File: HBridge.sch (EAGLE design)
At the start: 51 parts, among them IC1 74LS08D, IC2 A4954, J1 Inputs, J10 JUMPER_PTH, J11 PWM mode, J12 Fixed mode, J13 Ground, J14 5V, J15 Digital_8_13, J16 Analog, J17 Digital_0_7, J2 JUMPER_PTH, J3 JUMPER_PTH, J4 PWM mode, J5 Fixed mode, J6 Power, J7 Output A, J8 Output B, J9 JUMPER_PTH

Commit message: foo
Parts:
- removed C9: 100nF, freetronics:CAP0603
- removed J10, J9: JUMPER_PTH, freetronics-luke:JUMPER_PTH
- removed J11: PWM mode, freetronics-luke:JUMPER_PTH
- removed J12: Fixed mode, freetronics-luke:JUMPER_PTH
- removed J13: Ground, freetronics-master-v1:M08STD
- removed J14: 5V, freetronics-master-v1:M08STD
- removed J15: Digital_8_13, freetronics:M08
- removed J16: Analog, freetronics:M06SIP
- removed J17: Digital_0_7, freetronics:M08
- removed R10, R8, R9: 1k, freetronics-master-v1:RESISTOR0603
- removed R11, R12: 0.25R 1W, rcl:R-EU_R2010
- removed R13: 2K2, freetronics:RESISTOR0603
- removed R14: 10K, freetronics:RESISTOR0603
- removed S2: SWITCH, freetronics:TAC_SWITCHSMD
- added JP2: +5V, SparkFun:M07
- added JP3: (no value), freetronics-master-v1:M02PTH
- added RN1, RN2: 1K, freetronics-master-v1:4R-NCAY16
- added SJ1: Ch1 Fixed Current Select, freetronics-master-v1:SJ2W
- added SJ2: Ch2 Fixed Current Select, freetronics-master-v1:SJ2W
- added SJ3: Ch1 Fixed/PWM select, freetronics-master-v1:SJ2W
- added SJ4: Ch2 Fixed/PWM select, freetronics-master-v1:SJ2W
- C3: value 100 uF -> 100nF; device rcl:CPOL-EUE3.5-8 -> freetronics-master-v1:CAP0603
- C5: value 100nF -> 100 uF; device freetronics-master-v1:CAP0603 -> freetronics-master-v1:CAP_POLE
- IC1: value 74LS08D -> 74HC08D
- J1: value Inputs -> In 3/4; device freetronics-master-v1:M08STD -> freetronics-master-v1:M04PTH
- J2: value JUMPER_PTH -> Power; device freetronics-luke:JUMPER_PTH -> con-wago-508:W237-02P
- J3: value JUMPER_PTH -> In 1/2; device freetronics-luke:JUMPER_PTH -> freetronics-master-v1:M04PTH
- J4: value PWM mode -> Output A; device freetronics-luke:JUMPER_PTH -> con-wago-508:W237-02P; OC_FARNELL (none) -> unknown; OC_NEWARK (none) -> unknown
- J5: value Fixed mode -> Output B; device freetronics-luke:JUMPER_PTH -> con-wago-508:W237-02P; OC_FARNELL (none) -> unknown; OC_NEWARK (none) -> unknown
- J6: value Power -> Digital_8_13; device con-wago-508:W237-02P -> freetronics:M08
- J7: value Output A -> Analog; device con-wago-508:W237-02P -> freetronics:M06SIP; OC_FARNELL unknown -> (none); OC_NEWARK unknown -> (none)
- J8: value Output B -> Digital_0_7; device con-wago-508:W237-02P -> freetronics:M08; OC_FARNELL unknown -> (none); OC_NEWARK unknown -> (none)
- JP1: value SWITCH -> Gnd; device freetronics:M01PTH -> SparkFun:M07
- R1: value 1k -> 2K2
- R2: value 2k2 -> 2K2
- R3, R4: value 1k -> 10k
- R5, R6: value 1k -> 0.25R 1W; device freetronics-master-v1:RESISTOR0603 -> rcl:R-EU_R2010
- R7: value 2k2 -> 2K2; device freetronics-master-v1:RESISTOR0603 -> freetronics:RESISTOR0603
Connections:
- removed net N$249: JP1.1, R14.2, S2.3, S2.4
- removed net N$66: J10.2, R7.1
- removed net N$67: J10.1, J12.1, J9.1, R10.2
- removed net N$68: J9.2, R6.1
- removed net N$69: C5.1, J11.2, R9.2
- removed net N$83: C4.1, R8.2, R9.1
- new net N$1: RN2D.1, SJ2.2, SJ4.3
- new net N$2: C4.1, RN2B.1, SJ4.1
- new net N$20: RN2C.2, SJ2.3
- new net N$3: C3.1, RN2A.2, RN2B.2
- new net N$4: R1.1, SJ1.1
- net +5V: now also JP2.1, JP2.2, JP2.3, JP2.4, JP2.5, JP2.6, JP2.7, RN1C.1, RN2C.1; no longer C9.1, J14.1, J14.2, J14.3, J14.4, J14.5, J14.6, J14.7, J14.8, R6.2, R7.2, S2.1, S2.2
- net A0: now also J7.1; no longer J16.1
- net A1: now also J7.2; no longer J16.2
- net A2: now also J7.3; no longer J16.3
- net A3: now also J7.4; no longer J16.4
- net A4: now also J7.5; no longer J16.5
- net A5: now also J7.6; no longer J16.6
- net AREF: now also J6.8; no longer J15.8
- net D0_RX: now also J8.1; no longer J17.1
- net D10: now also J6.3; no longer J15.3
- net D11_MOSI: now also J6.4; no longer J15.4
- net D12_MISO: now also J6.5; no longer J15.5
- net D13_SCK: now also J6.6; no longer J15.6
- net D1_TX: now also J8.2; no longer J17.2
- net D2: now also J8.3; no longer J17.3
- net D3: now also J8.4; no longer J17.4
- net D4: now also J8.5; no longer J17.5
- net D5: now also J8.6; no longer J17.6
- net D6: now also J8.7; no longer J17.7
- net D7: now also J8.8; no longer J17.8
- net D8: now also J6.1; no longer J15.1
- net D9: now also J6.2; no longer J15.2
- net GND: now also C3.2, C5.-, J2-2.KL, J6.7, JP1.1, JP1.2, JP1.3, JP1.4, JP1.5, JP1.6, JP1.7, R3.1, R4.1, R6.1, R7.2, RN1D.2, RN2D.2; no longer C3.-, C5.2, C9.2, J13.1, J13.2, J13.3, J13.4, J13.5, J13.6, J13.7, J13.8, J15.7, J6-2.KL, R10.1, R11.1, R12.1, R13.2, R14.1
- net IN1: now also J3.1; no longer J1.1
- net IN2: now also J3.2; no longer J1.2
- net IN3: now also J1.1; no longer J1.3
- net IN4: now also J1.2; no longer J1.4
- net N$10: now also J4-2.KL; no longer J7-2.KL
- net N$11: now also J5-1.KL; no longer J8-1.KL
- net N$12: now also J5-2.KL; no longer J8-2.KL
- net N$13: now also R5.2; no longer R11.2
- net N$14: now also R6.2; no longer R12.2
- net N$15: now also RN1C.2, SJ1.3; no longer J3.2, R2.1
- net N$16: now also RN1D.1, SJ1.2, SJ3.3; no longer J2.1, J3.1, J5.1, R5.2
- net N$17: now also R2.1, SJ2.1; no longer J2.2, R1.1
- net N$18: now also RN1B.1, SJ3.1; no longer J4.2, R4.2
- net N$19: now also RN1A.2, RN1B.2; no longer R3.2, R4.1
- net N$248: now also R7.1; no longer R13.1
- net N$9: now also J4-1.KL; no longer J7-1.KL
- net PWM12: now also J3.3, R3.2; no longer J1.5
- net PWM34: now also J1.3, R4.2; no longer J1.6
- net REF_PWM_12: now also J3.4, RN1A.1; no longer J1.7, R3.1
- net REF_PWM_34: now also J1.4, RN2A.1; no longer J1.8, R8.1
- net VBB: now also C5.+, J2-1.KL, JP3.2; no longer C3.+, J6-1.KL
- net VIN: now also JP3.1
- net VREF12: now also SJ3.2; no longer J4.1, J5.2
- net VREF34: now also SJ4.2; no longer J11.1, J12.2
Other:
- note added: "1-2-3: 2.96V, I = 1.19A"
- note added: "1-2: 1.56V, I = 625mA"
- note added: "1k resistor networks: Small SMD 4-way resistor pack, SAME package footprint as EM."
- note added: "2-3: 2.5V, I = 1A"
- note added: "I limit = Vref / (0.25 ohms * 10)"
- note removed: "Both in: 2.96 V"
- note removed: "C3: Large through-hole electrolytic"
- note removed: "J12 in: 1.56 V"
- note removed: "J13 in: 2.5 V"
- note removed: "J8 in: 1.56 V"
- note removed: "J9 in: 2.5 V"
- moved on the sheet: C1, C2, C4, C6, C7, C8, IC1A, IC1B, IC1C, IC1D, IC1P, IC2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

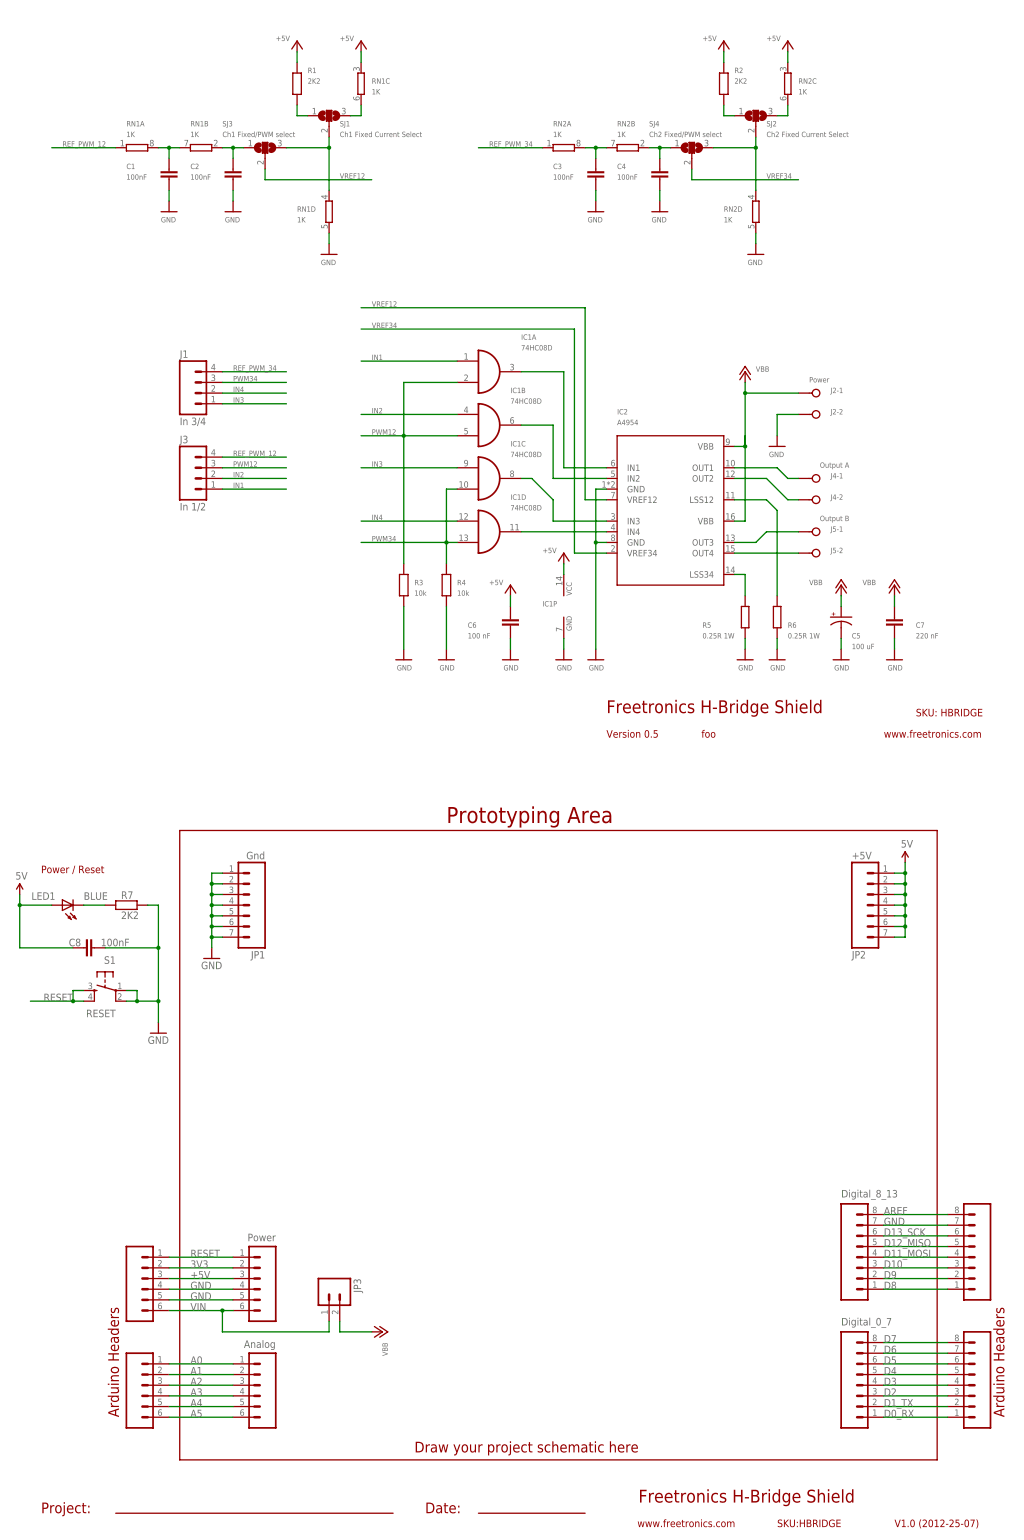
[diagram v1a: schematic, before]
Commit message: Added ICSP header for R3
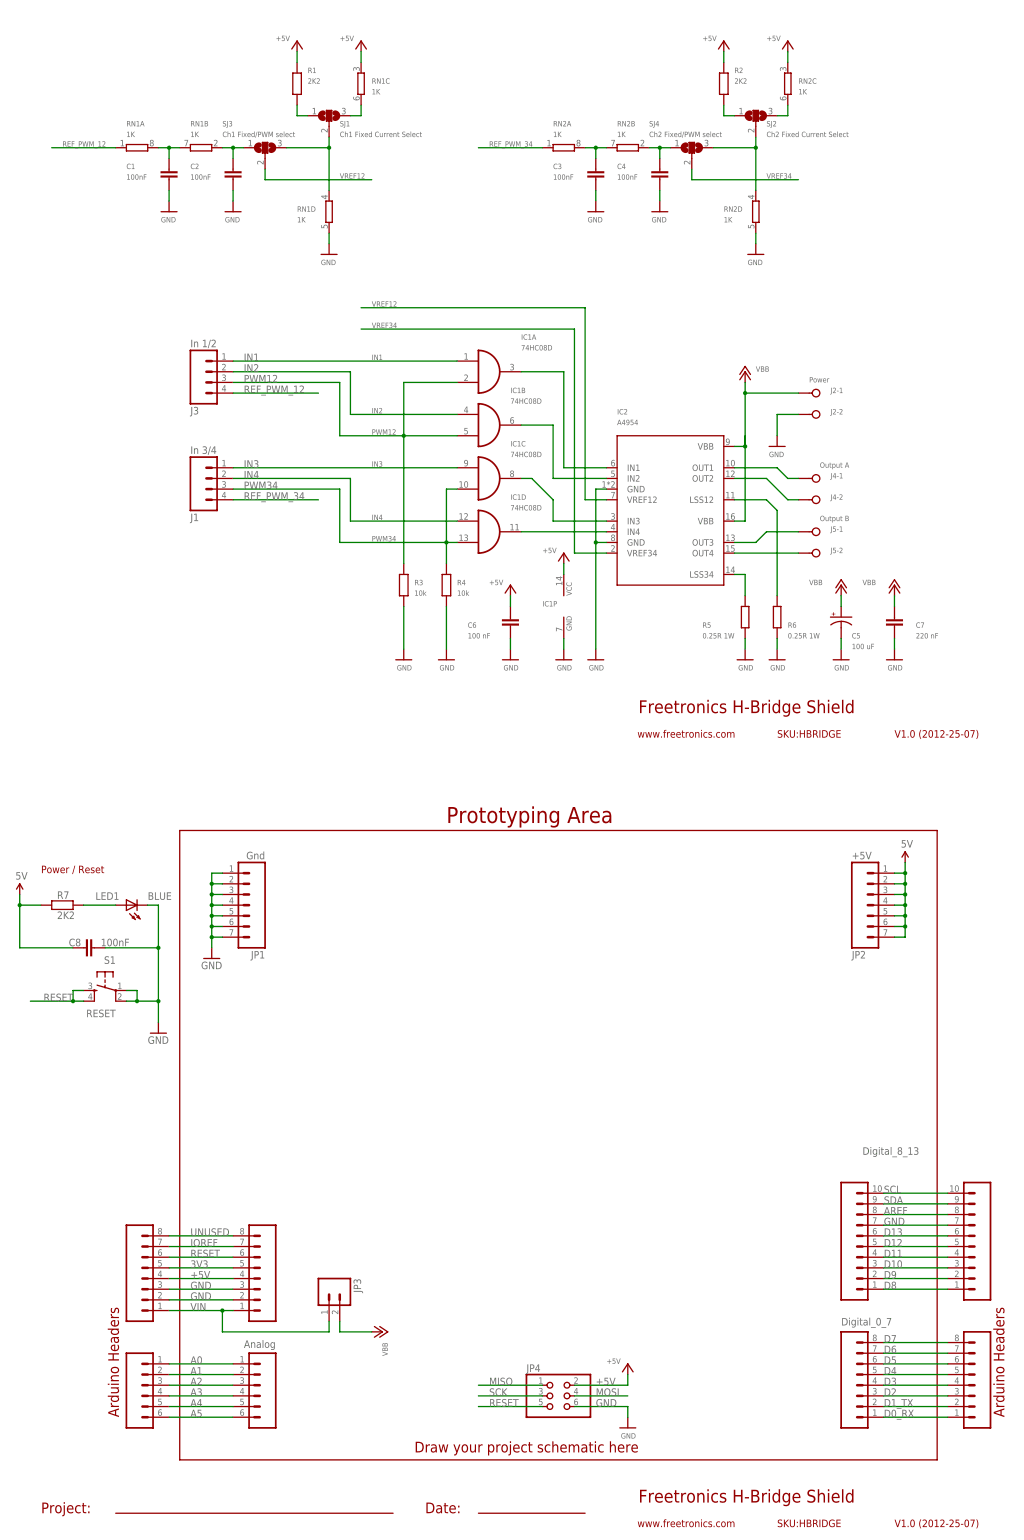
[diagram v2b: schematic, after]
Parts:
- removed POWER, SLP: Power, freetronics:M06SIP
- added JP4: (no value), freetronics-master-v1:PINHD-2X3
- added SL4, SL5: Digital_0_7, freetronics:M08
- J6, SL1: device freetronics:M08 -> freetronics-original:M100.1
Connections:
- net D11_MOSI renamed D11
- net D12_MISO renamed D12
- net D13_SCK renamed D13
- removed net N$248: LED1.C, R7.1
- new net IOREF: SL4.7, SL5.7
- new net MISO: JP4.1
- new net MOSI: JP4.4
- new net N$22: LED1.A, R7.2
- new net SCK: JP4.3
- new net SCL: J6.10, SL1.10
- new net SDA: J6.9, SL1.9
- new net UNUSED: SL4.8, SL5.8
- net +5V: now also JP4.2, R7.1, SL4.4, SL5.4; no longer LED1.A, POWER.3, SLP.3
- net 3V3: now also SL4.5, SL5.5; no longer POWER.2, SLP.2
- net GND: now also JP4.6, LED1.C, SL4.2, SL4.3, SL5.2, SL5.3; no longer POWER.4, POWER.5, R7.2, SLP.4, SLP.5
- net RESET: now also JP4.5, SL4.6, SL5.6; no longer POWER.1, SLP.1
- net VIN: now also SL4.1, SL5.1; no longer POWER.6, SLP.6
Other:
- note removed: "SKU: HBRIDGE"
- note removed: "Version 0.5"
- note removed: "foo"
- moved on the sheet: J1, J3, LED1, R7

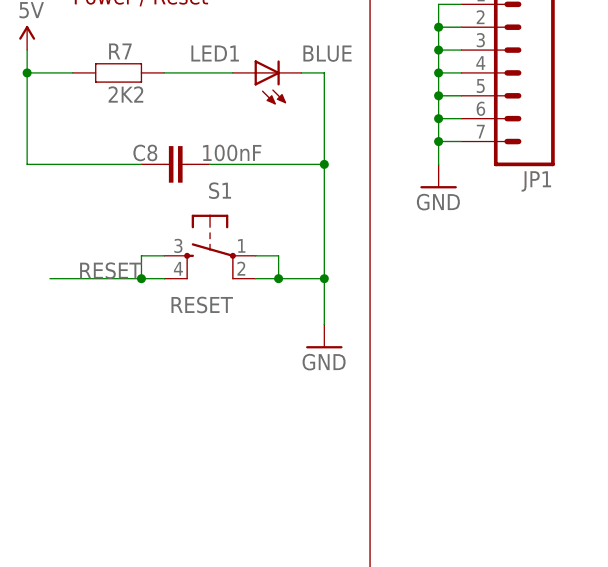
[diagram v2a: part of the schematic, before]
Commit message: Replaced reset button with smaller 2-pin version
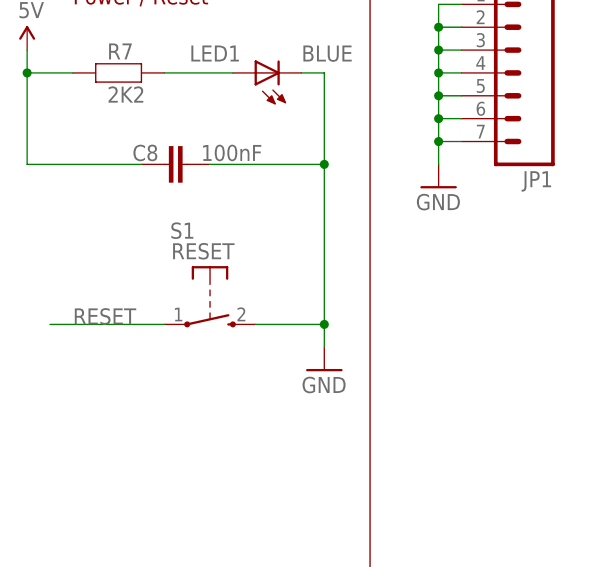
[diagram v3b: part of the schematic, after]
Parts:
- S1: device freetronics:TAC_SWITCHSMD -> freetronics-master-v1:TAC_SWITCH_2PIN
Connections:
- net GND: now also S1.S; no longer S1.1, S1.2
- net RESET: now also S1.P; no longer S1.3, S1.4
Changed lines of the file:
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@@
 <part name="SL3" library="freetronics" deviceset="M08" device="" value="Digital_0_7"/>
 <part name="C8" library="freetronics" deviceset="CAP" device="0603" value="100nF"/>
-<part name="S1" library="freetronics" deviceset="TAC_SWITCH" device="SMD" value="RESET"/>
 <part name="U$2" library="freetronics" deviceset="5V" device=""/>
 <part name="U$3" library="freetronics" deviceset="5V" device=""/>
@@
 <part name="U$18" library="freetronics-luke" deviceset="GND" device=""/>
 <part name="U$26" library="freetronics-luke" deviceset="+5V" device=""/>
+<part name="S1" library="freetronics-master-v1" deviceset="TAC_SWITCH_2PIN" device="" value="RESET"/>
 </parts>
 <sheets>
@@
 <attribute name="VALUE" x="26.924" y="145.161" size="1.778" layer="96"/>
 </instance>
-<instance part="S1" gate="S" x="27.94" y="134.62" rot="MR0"/>
 <instance part="U$2" gate="G$1" x="7.62" y="157.48"/>
 <instance part="U$3" gate="G$1" x="218.44" y="165.1"/>
@@
 <attribute name="VALUE" x="16.51" y="151.638" size="1.778" layer="96"/>
 </instance>
-<instance part="GND4" gate="1" x="40.64" y="124.46"/>
+<instance part="GND4" gate="1" x="40.64" y="121.92"/>
 <instance part="IC2" gate="G$1" x="162.56" y="248.92" smashed="yes">
 <attribute name="NAME" x="149.86" y="271.78" size="1.27" layer="95"/>
@@
 <attribute name="VALUE" x="147.32" y="45.72" size="1.27" layer="96"/>
 </instance>
+<instance part="S1" gate="1" x="27.94" y="127"/>
 </instances>
 <busses>
@@
 <wire x1="40.64" y1="144.78" x2="40.64" y2="154.94" width="0.1524" layer="91"/>
 <wire x1="27.94" y1="144.78" x2="40.64" y2="144.78" width="0.1524" layer="91"/>
-<wire x1="40.64" y1="132.08" x2="40.64" y2="144.78" width="0.1524" layer="91"/>
-<wire x1="35.56" y1="132.08" x2="33.02" y2="132.08" width="0.1524" layer="91"/>
-<wire x1="33.02" y1="134.62" x2="35.56" y2="134.62" width="0.1524" layer="91"/>
-<wire x1="35.56" y1="134.62" x2="35.56" y2="132.08" width="0.1524" layer="91"/>
-<wire x1="35.56" y1="132.08" x2="40.64" y2="132.08" width="0.1524" layer="91"/>
-<wire x1="40.64" y1="132.08" x2="40.64" y2="127" width="0.1524" layer="91"/>
+<wire x1="40.64" y1="127" x2="40.64" y2="144.78" width="0.1524" layer="91"/>
+<wire x1="33.02" y1="127" x2="40.64" y2="127" width="0.1524" layer="91"/>
+<wire x1="40.64" y1="127" x2="40.64" y2="124.46" width="0.1524" layer="91"/>
 <junction x="40.64" y="144.78"/>
-<junction x="35.56" y="132.08"/>
-<junction x="40.64" y="132.08"/>
+<junction x="40.64" y="127"/>
 <pinref part="C8" gate="G$1" pin="2"/>
-<pinref part="S1" gate="S" pin="2"/>
-<pinref part="S1" gate="S" pin="1"/>
 <pinref part="GND4" gate="1" pin="GND"/>
 <pinref part="LED1" gate="G$1" pin="C"/>
 <wire x1="40.64" y1="154.94" x2="38.1" y2="154.94" width="0.1524" layer="91"/>
+<pinref part="S1" gate="1" pin="S"/>
 </segment>
 <segment>
@@
 </segment>
 <segment>
-<wire x1="22.86" y1="134.62" x2="20.32" y2="134.62" width="0.1524" layer="91"/>
-<wire x1="20.32" y1="134.62" x2="20.32" y2="132.08" width="0.1524" layer="91"/>
-<wire x1="20.32" y1="132.08" x2="22.86" y2="132.08" width="0.1524" layer="91"/>
-<wire x1="20.32" y1="132.08" x2="10.16" y2="132.08" width="0.1524" layer="91"/>
-<junction x="20.32" y="132.08"/>
-<label x="20.32" y="132.08" size="1.778" layer="95" rot="MR0"/>
-<pinref part="S1" gate="S" pin="3"/>
-<pinref part="S1" gate="S" pin="4"/>
-</segment>
-<segment>
+<wire x1="22.86" y1="127" x2="10.16" y2="127" width="0.1524" layer="91"/>
+<label x="12.7" y="127" size="1.778" layer="95"/>
+<pinref part="S1" gate="1" pin="P"/>
+</segment>
+<segment>
